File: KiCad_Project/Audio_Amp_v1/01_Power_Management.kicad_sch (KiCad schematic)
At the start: 0 parts

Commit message: Add power amplifier schematic, custom library, and initial components
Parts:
- added IC1: LMR33630BDDA, SOIC127P600X170-9N, symbol LMR33630BDDA:LMR33630BDDA
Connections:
- new net GNDA: IC1.9 (AGND)
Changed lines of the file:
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@@
 	(generator_version "9.0")
 	(paper "A4")
+	(wire
+		(pts
+			(xy 104.14 90.17) (xy 104.14 87.63)
+		)
+		(stroke
+			(width 0)
+			(type default)
+		)
+	)
+	(symbol
+		(lib_id "power:GNDA")
+		(at 104.14 90.17 0)
+		(unit 1)
+		(exclude_from_sim no)
+		(in_bom yes)
+		(on_board yes)
+		(dnp no)
+		(fields_autoplaced yes)
+		(property "Reference" "#PWR01"
+			(at 104.14 96.52 0)
+			(effects
+				(font
+					(size 1.27 1.27)
+				)
+				(hide yes)
+			)
+		)
+		(property "Value" "GNDA"
+			(at 104.14 95.25 0)
+			(effects
+				(font
+					(size 1.27 1.27)
+				)
+			)
+		)
+		(property "Footprint" ""
+			(at 104.14 90.17 0)
+			(effects
+				(font
+					(size 1.27 1.27)
+				)
+				(hide yes)
+			)
+		)
+		(property "Datasheet" ""
+			(at 104.14 90.17 0)
+			(effects
+				(font
+					(size 1.27 1.27)
+				)
+				(hide yes)
+			)
+		)
+		(property "Description" "Power symbol creates a global label with name \"GNDA\" , analog ground"
+			(at 104.14 90.17 0)
+			(effects
+				(font
+					(size 1.27 1.27)
+				)
+				(hide yes)
+			)
+		)
+		(pin "1"
+		)
+		(instances
+			(project ""
+				(path "/d992164b-b1d0-4285-be2c-12a40c17e5cc/137e5605-a318-4b34-aabf-8cb0f4de8d0a"
+					(reference "#PWR01")
+					(unit 1)
+				)
+			)
+		)
+	)
+	(symbol
+		(lib_id "LMR33630BDDA:LMR33630BDDA")
+		(at 88.9 64.77 0)
+		(unit 1)
+		(exclude_from_sim no)
+		(in_bom yes)
+		(on_board yes)
+		(dnp no)
+		(fields_autoplaced yes)
+		(property "Reference" "IC1"
+			(at 104.14 57.15 0)
+			(effects
+				(font
+					(size 1.27 1.27)
+				)
+			)
+		)
+		(property "Value" "LMR33630BDDA"
+			(at 104.14 59.69 0)
+			(effects
+				(font
+					(size 1.27 1.27)
+				)
+			)
+		)
+		(property "Footprint" "SOIC127P600X170-9N"
+			(at 115.57 159.69 0)
+			(effects
+				(font
+					(size 1.27 1.27)
+				)
+				(justify left top)
+				(hide yes)
+			)
+		)
+		(property "Datasheet" "http://www.ti.com/lit/gpn/LMR33630"
+			(at 115.57 259.69 0)
+			(effects
+				(font
+					(size 1.27 1.27)
+				)
+				(justify left top)
+				(hide yes)
+			)
+		)
+		(property "Description" "SIMPLE SWITCHER 3.8V to 36V, 3A Synchronous Buck Converter With Ultra-Low EMI"
+			(at 88.9 64.77 0)
+			(effects
+				(font
+					(size 1.27 1.27)
+				)
+				(hide yes)
+			)
+		)
+		(property "Height" "1.7"
+			(at 115.57 459.69 0)
+			(effects
+				(font
+					(size 1.27 1.27)
+				)
+				(justify left top)
+				(hide yes)
+			)
+		)
+		(property "Mouser Part Number" "595-LMR33630BDDA"
+			(at 115.57 559.69 0)
+			(effects
+				(font
+					(size 1.27 1.27)
+				)
+				(justify left top)
+				(hide yes)
+			)
+		)
+		(property "Mouser Price/Stock" "https://www.mouser.co.uk/ProductDetail/Texas-Instruments/LMR33630BDDA?qs=r5DSvlrkXmJSaC%2FkFkJm9Q%3D%3D"
+			(at 115.57 659.69 0)
+			(effects
+				(font
+					(size 1.27 1.27)
+				)
+				(justify left top)
+				(hide yes)
+			)
+		)
+		(property "Manufacturer_Name" "Texas Instruments"
+			(at 115.57 759.69 0)
+			(effects
+				(font
+					(size 1.27 1.27)
+				)
+				(justify left top)
+				(hide yes)
+			)
+		)
+		(property "Manufacturer_Part_Number" "LMR33630BDDA"
+			(at 115.57 859.69 0)
+			(effects
+				(font
+					(size 1.27 1.27)
+				)
+				(justify left top)
+				(hide yes)
+			)
+		)
+		(pin "5"
+		)
+		(pin "3"
+		)
+		(pin "1"
+		)
+		(pin "2"
+		)
+		(pin "9"
+		)
+		(pin "4"
+		)
+		(pin "7"
+		)
+		(pin "8"
+		)
+		(pin "6"
+		)
+		(instances
+			(project ""
+				(path "/d992164b-b1d0-4285-be2c-12a40c17e5cc/137e5605-a318-4b34-aabf-8cb0f4de8d0a"
+					(reference "IC1")
+					(unit 1)
+				)
+			)
+		)
+	)
 )

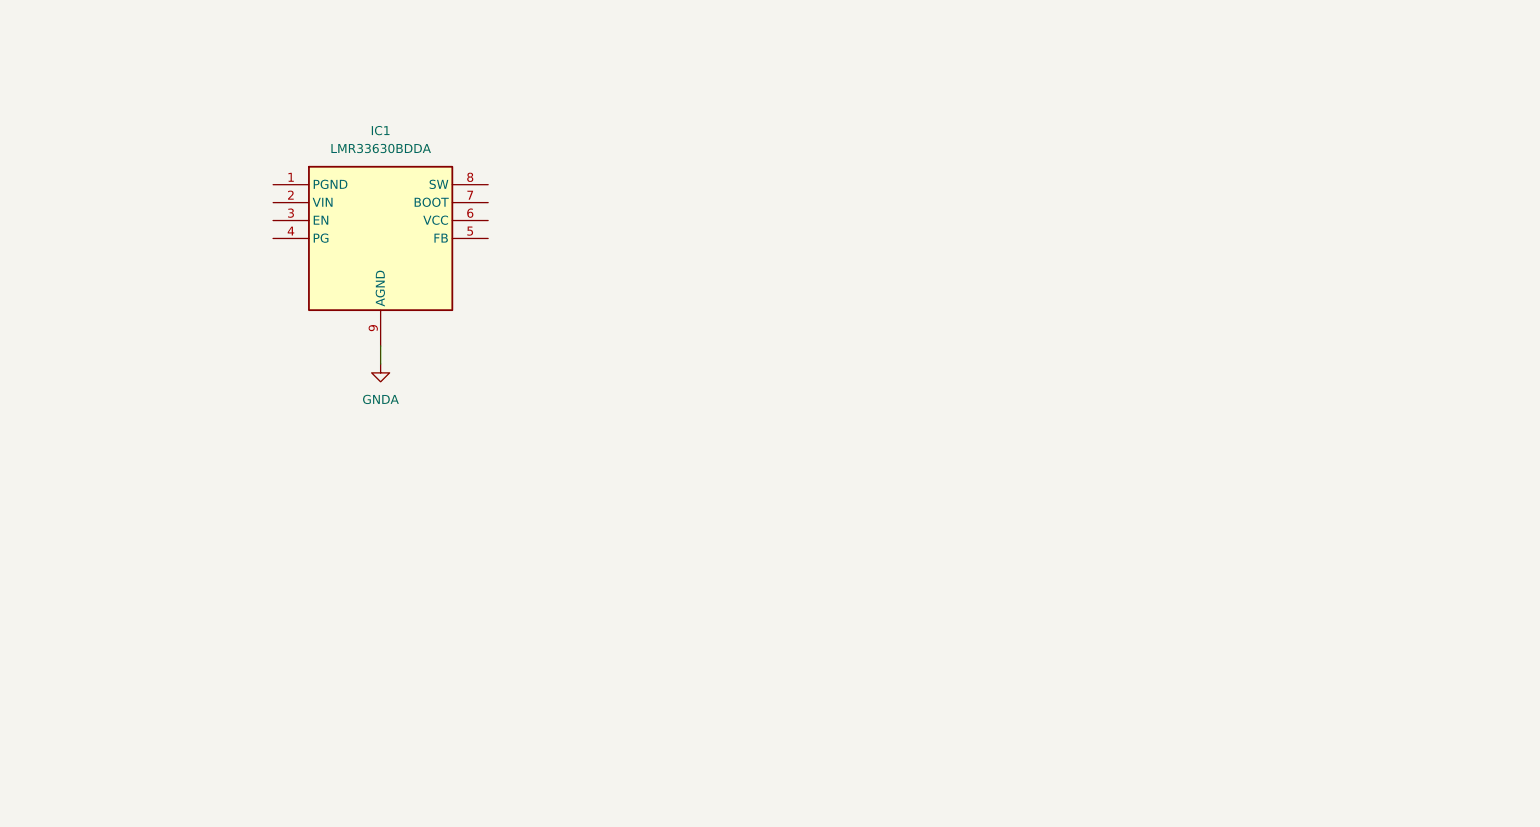
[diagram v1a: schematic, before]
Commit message: Updated Power management section, Bluetooth receiver and connectors. Added some components footprints and 3D.
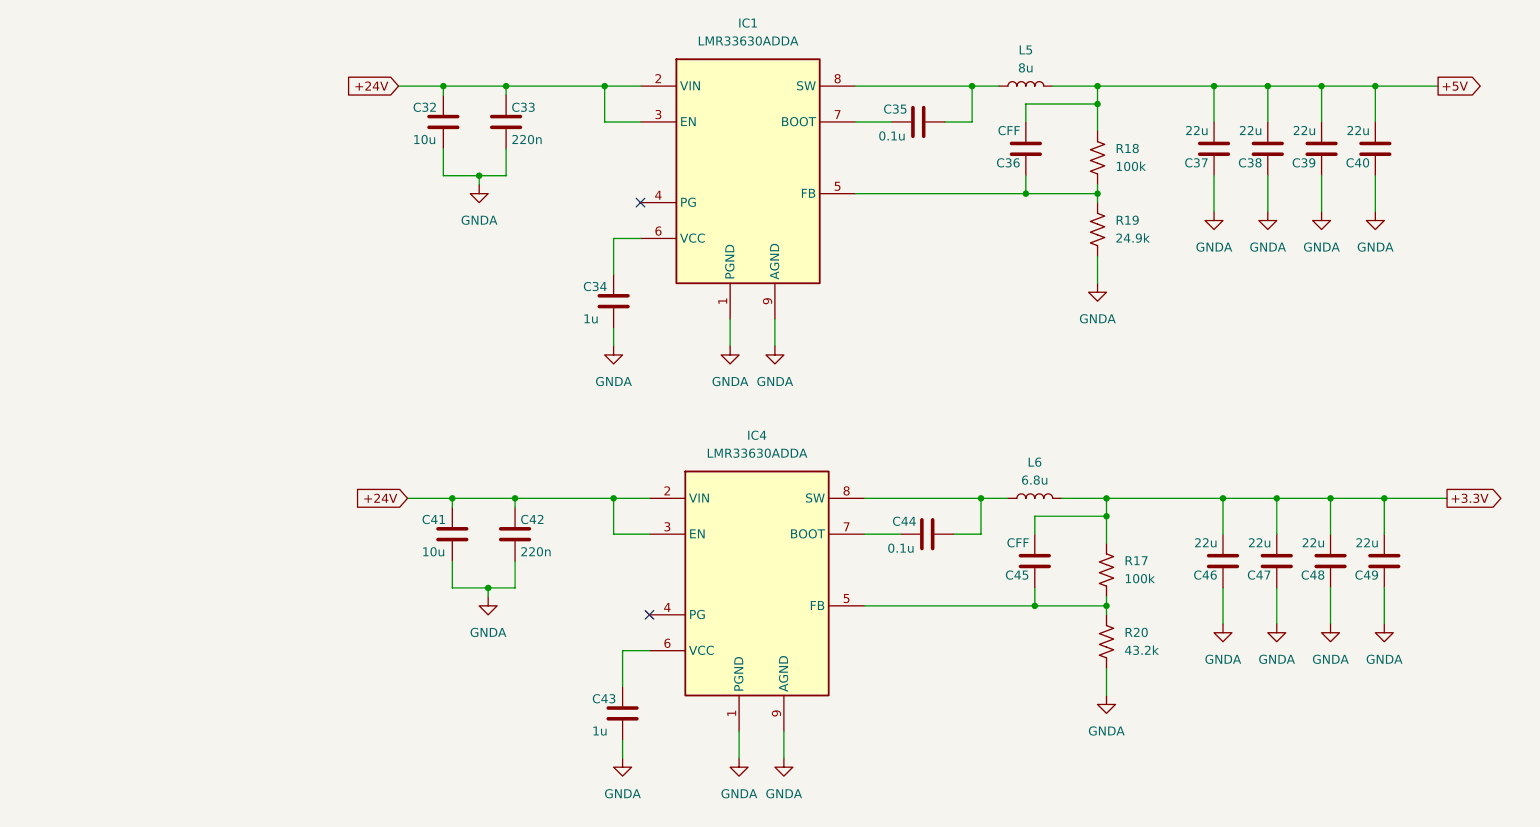
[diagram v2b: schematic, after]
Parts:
- added C32, C41: 10u, symbol Device:C
- added C33, C42: 220n, symbol Device:C
- added C34, C43: 1u, symbol Device:C
- added C35, C44: 0.1u, symbol Device:C
- added C36, C45: CFF, symbol Device:C
- added C37, C38, C39, C40, C46, C47, C48, C49: 22u, symbol Device:C
- added IC4: LMR33630ADDA, SOIC127P600X170-9N, symbol LMR33630BDDA:LMR33630BDDA
- added L5: 8u, symbol Device:L
- added L6: 6.8u, symbol Device:L
- added R17, R18: 100k, symbol Device:R_US
- added R19: 24.9k, symbol Device:R_US
- added R20: 43.2k, symbol Device:R_US
- IC1: value LMR33630BDDA -> LMR33630ADDA
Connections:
- net GNDA: now also IC1.1 (PGND), C32.2, C33.2, C34.2, C37.1, C38.1, C39.1, C40.1, C41.2, C42.2, C43.2, C46.1, C47.1, C48.1, C49.1, IC4.1 (PGND), IC4.9 (AGND), R19.1, R20.1
- net +24V: now reaches IC1.2 (VIN)
- net +24V: now also IC1.3 (EN), C32.1, C33.1, C41.1, C42.1, IC4.2 (VIN), IC4.3 (EN)
- net at IC1.5 (FB): now also C36.1, R18.1, R19.2
- net at IC1.6 (VCC): now also C34.1
- net at IC1.7 (BOOT): now also C35.1
- net at IC1.8 (SW): now also C35.2, L5.1
- new net: C44.1, IC4.7 (BOOT)
- new net: C44.2, IC4.8 (SW), L6.1
- new net: C43.1, IC4.6 (VCC)
- new net: C45.1, IC4.5 (FB), R17.1, R20.2
- new net +3.3V: C45.2, C46.2, C47.2, C48.2, C49.2, L6.2, R17.2
- new net +5V: C36.2, C37.2, C38.2, C39.2, C40.2, L5.2, R18.2
- no-connect marks 0 -> 2
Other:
- moved on the sheet: IC1

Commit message: Remove KiCad .history from tracking, add to gitignore
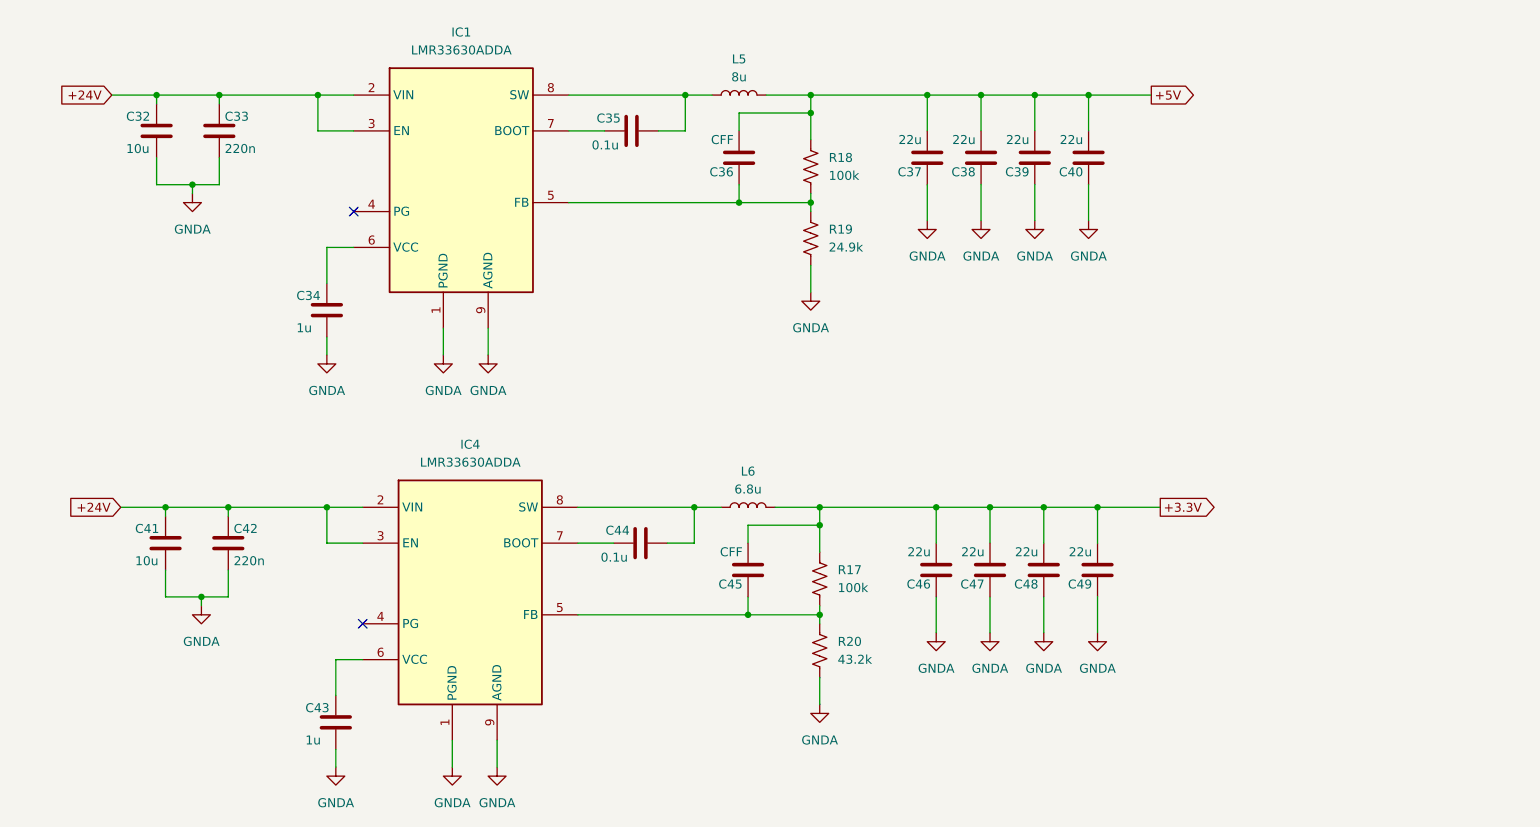
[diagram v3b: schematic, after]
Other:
- moved on the sheet: C32, C33, C34, C35, C36, C37, C38, C39, C40, C41, C42, C43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

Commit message: Finished Schematic and started Layout
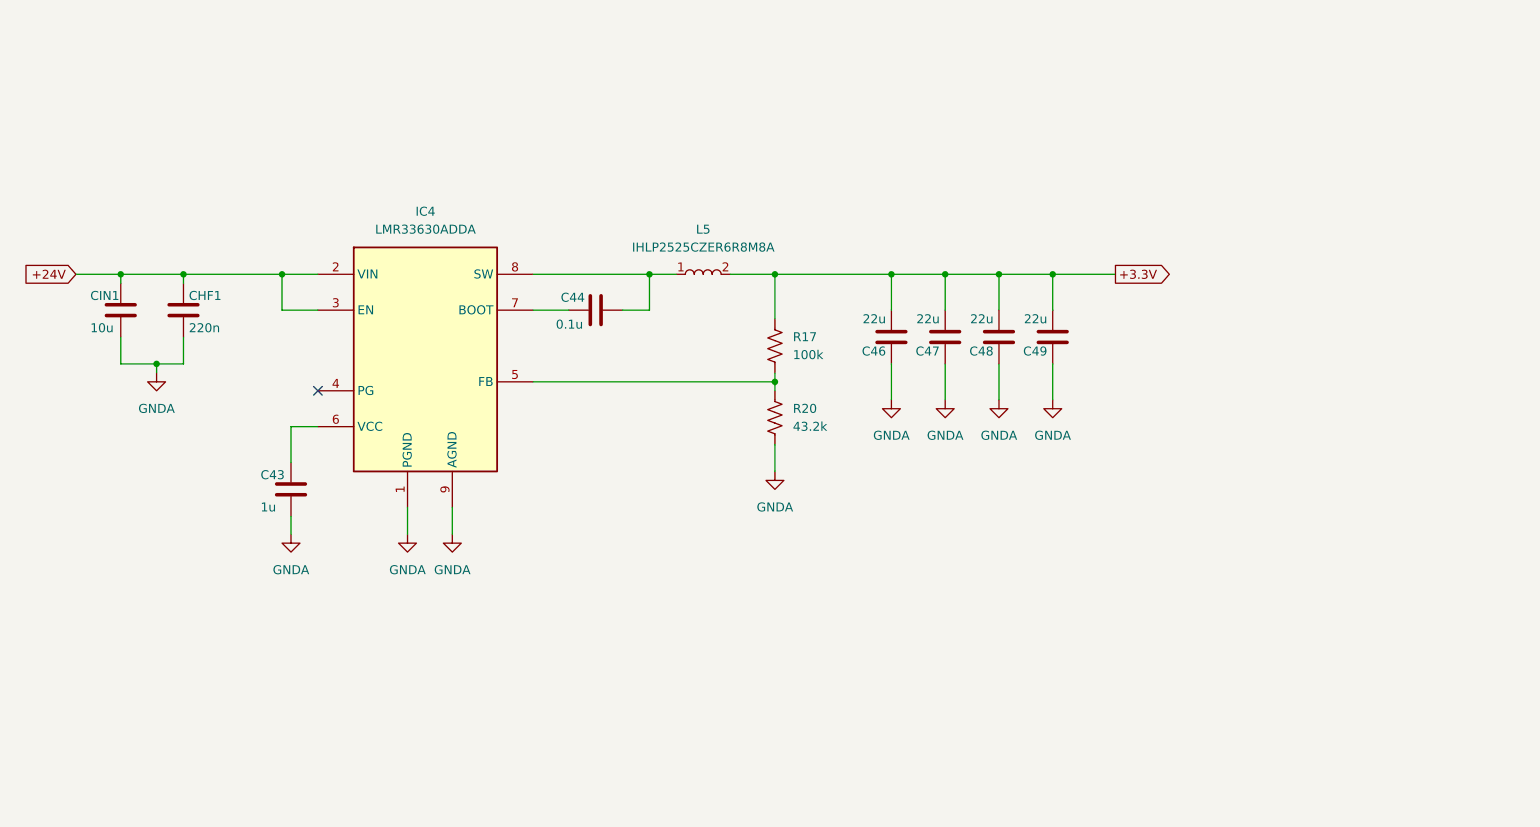
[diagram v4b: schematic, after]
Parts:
- removed C32: 10u, symbol Device:C
- removed C33: 220n, symbol Device:C
- removed C34: 1u, symbol Device:C
- removed C35: 0.1u, symbol Device:C
- removed C36, C45: CFF, symbol Device:C
- removed C37, C38, C39, C40: 22u, symbol Device:C
- removed IC1: LMR33630ADDA, SOIC127P600X170-9N, symbol LMR33630BDDA:LMR33630BDDA
- removed L5: 8u, symbol Device:L
- removed L6: 6.8u, symbol Device:L
- removed R18: 100k, symbol Device:R_US
- removed R19: 24.9k, symbol Device:R_US
- added L5: IHLP2525CZER6R8M8A, IHLP2525CZER6R8M8A:INDPM6965X300N, symbol IHLP2525CZER6R8M8A:IHLP2525CZER6R8M8A
- C43, C44: footprint (none) -> Capacitor_SMD:C_0603_1608Metric
- C46, C47, C48, C49: footprint (none) -> Capacitor_SMD:C_0805_2012Metric
- CHF1: renamed from C42; footprint (none) -> Capacitor_SMD:C_0805_2012Metric
- CIN1: renamed from C41; footprint (none) -> Capacitor_SMD:C_1206_3216Metric
- R17, R20: footprint (none) -> Resistor_SMD:R_0603_1608Metric
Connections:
- net +3.3V: now also L5.2
- net at C44.2, IC4.8 (SW): now also L5.1
- no-connect marks 2 -> 1
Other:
- moved on the sheet: C43, C44, C46, CHF1, CIN1, IC4, R17, R20

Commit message: Continued Layout
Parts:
- added TP3, TP4: TestPoint, TestPoint:TestPoint_Pad_D2.0mm, symbol Connector:TestPoint
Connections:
- net +24V: now also TP4.1
- net +3.3V: now also TP3.1
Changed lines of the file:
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@@
+	(wire
+		(pts
+			(xy 233.68 93.98) (xy 233.68 86.36)
+		)
+		(stroke
+			(width 0)
+			(type default)
+		)
+	)
 	(wire
 		(pts
@@
 	(wire
 		(pts
+			(xy 252.73 93.98) (xy 252.73 86.36)
+		)
+		(stroke
+			(width 0)
+			(type default)
+		)
+	)
+	(wire
+		(pts
 			(xy 91.44 114.3) (xy 91.44 111.76)
 		)
@@
 			(width 0)
 			(type default)
+		)
+	)
+	(label "+24V"
+		(at 252.73 93.98 0)
+		(effects
+			(font
+				(size 1.27 1.27)
+			)
+			(justify left bottom)
+		)
+	)
+	(label "+3.3V"
+		(at 233.68 93.98 0)
+		(effects
+			(font
+				(size 1.27 1.27)
+			)
+			(justify left bottom)
 		)
 	)
@@
 	)
 	(symbol
+		(lib_id "Connector:TestPoint")
+		(at 252.73 86.36 0)
+		(unit 1)
+		(body_style 1)
+		(exclude_from_sim no)
+		(in_bom yes)
+		(on_board yes)
+		(in_pos_files yes)
+		(dnp no)
+		(fields_autoplaced yes)
+		(property "Reference" "TP4"
+			(at 255.27 81.7879 0)
+			(show_name no)
+			(do_not_autoplace no)
+			(effects
+				(font
+					(size 1.27 1.27)
+				)
+				(justify left)
+			)
+		)
+		(property "Value" "TestPoint"
+			(at 255.27 84.3279 0)
+			(show_name no)
+			(do_not_autoplace no)
+			(effects
+				(font
+					(size 1.27 1.27)
+				)
+				(justify left)
+			)
+		)
+		(property "Footprint" "TestPoint:TestPoint_Pad_D2.0mm"
+			(at 257.81 86.36 0)
+			(hide yes)
+			(show_name no)
+			(do_not_autoplace no)
+			(effects
+				(font
+					(size 1.27 1.27)
+				)
+			)
+		)
+		(property "Datasheet" ""
+			(at 257.81 86.36 0)
+			(hide yes)
+			(show_name no)
+			(do_not_autoplace no)
+			(effects
+				(font
+					(size 1.27 1.27)
+				)
+			)
+		)
+		(property "Description" "test point"
+			(at 252.73 86.36 0)
+			(hide yes)
+			(show_name no)
+			(do_not_autoplace no)
+			(effects
+				(font
+					(size 1.27 1.27)
+				)
+			)
+		)
+		(pin "1"
+		)
+		(instances
+			(project "Audio_Amp_v1"
+				(path "/d992164b-b1d0-4285-be2c-12a40c17e5cc/137e5605-a318-4b34-aabf-8cb0f4de8d0a"
+					(reference "TP4")
+					(unit 1)
+				)
+			)
+		)
+	)
+	(symbol
 		(lib_id "power:GNDA")
 		(at 72.39 91.44 0)
@@
 					(unit 1)
 				)
+			)
+		)
+	)
+	(symbol
+		(lib_id "Connector:TestPoint")
+		(at 233.68 86.36 0)
+		(unit 1)
+		(body_style 1)
+		(exclude_from_sim no)
+		(in_bom yes)
+		(on_board yes)
+		(in_pos_files yes)
+		(dnp no)
+		(fields_autoplaced yes)
+		(property "Reference" "TP3"
+			(at 236.22 81.7879 0)
+			(show_name no)
+			(do_not_autoplace no)
+			(effects
+				(font
+					(size 1.27 1.27)
+				)
+				(justify left)
+			)
+		)
+		(property "Value" "TestPoint"
+			(at 236.22 84.3279 0)
+			(show_name no)
+			(do_not_autoplace no)
+			(effects
+				(font
+					(size 1.27 1.27)
+				)
+				(justify left)
+			)
+		)
+		(property "Footprint" "TestPoint:TestPoint_Pad_D2.0mm"
+			(at 238.76 86.36 0)
+			(hide yes)
+			(show_name no)
+			(do_not_autoplace no)
+			(effects
+				(font
+					(size 1.27 1.27)
+				)
+			)
+		)
+		(property "Datasheet" ""
+			(at 238.76 86.36 0)
+			(hide yes)
+			(show_name no)
+			(do_not_autoplace no)
+			(effects
+				(font
+					(size 1.27 1.27)
+				)
+			)
+		)
+		(property "Description" "test point"
+			(at 233.68 86.36 0)
+			(hide yes)
+			(show_name no)
+			(do_not_autoplace no)
+			(effects
+				(font
+					(size 1.27 1.27)
+				)
+			)
+		)
+		(pin "1"
+		)
+		(instances
+			(project "Audio_Amp_v1"
+				(path "/d992164b-b1d0-4285-be2c-12a40c17e5cc/137e5605-a318-4b34-aabf-8cb0f4de8d0a"
+					(reference "TP3")
+					(unit 1)
+				)
